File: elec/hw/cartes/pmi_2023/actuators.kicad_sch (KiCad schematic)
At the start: 39 parts, among them J1 con_servo, J2 con_servo, J3 con_servo, J4 con_servo, U17 SN74LVC2T45DCU, U21 SN74LVC2T45DCU, U23 PCA9685PW

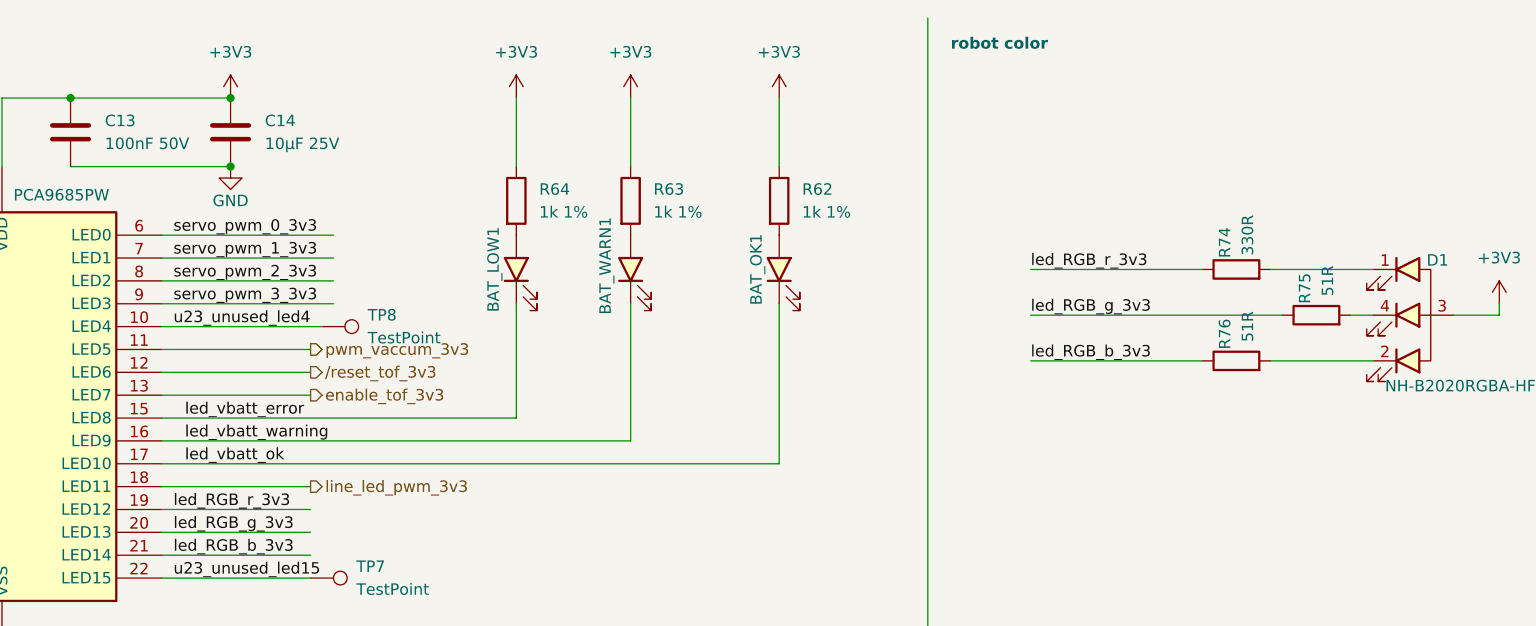
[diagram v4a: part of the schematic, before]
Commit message: bom updated and component selection optimized to decrease bom cost
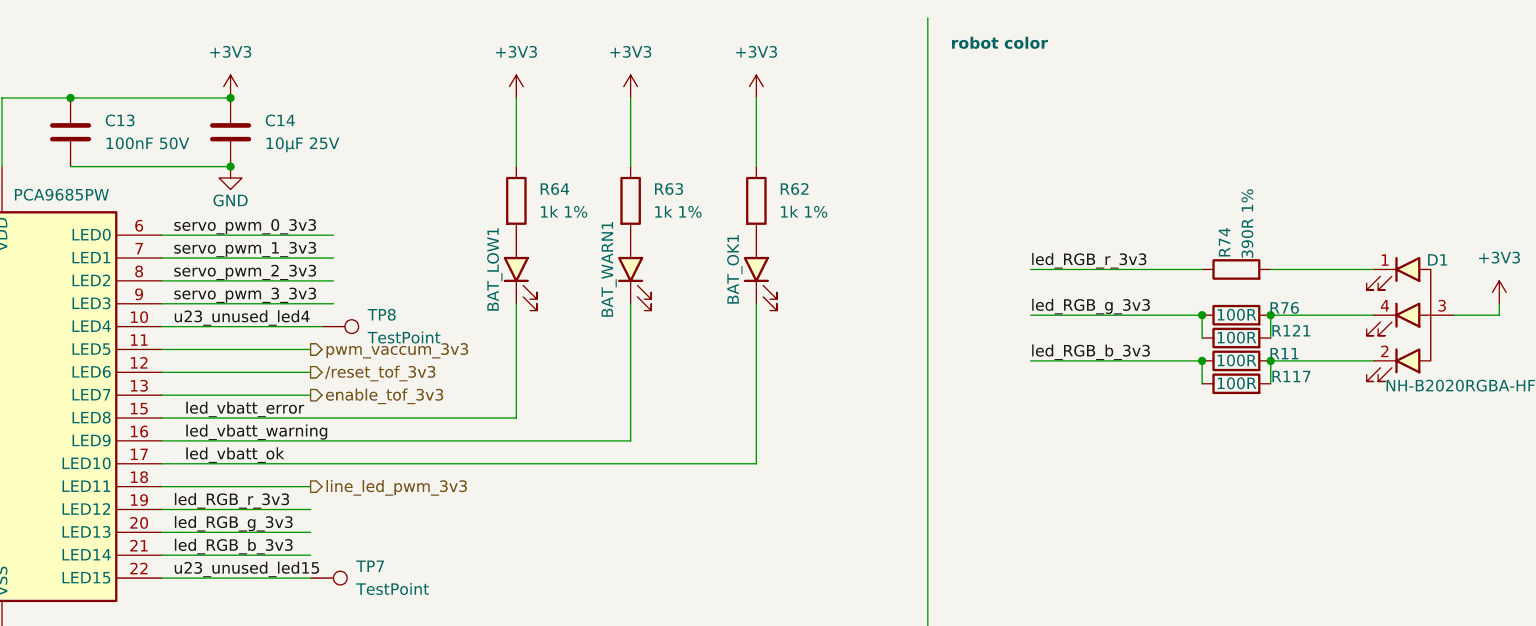
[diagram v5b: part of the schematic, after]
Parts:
- removed R75, R76: 51R, cocotter_resistor:r0603_reflow, symbol cocotter_resistors:R_51R_0603_1%
- added R11, R117, R121, R76: 100R, cocotter_resistor:r0603_reflow, symbol cocotter_resistors:R_100R_0603_1%
- BAT_OK1: value white, 0603 -> green, 0603; symbol cocotter_diodes:white_led_0603 -> cocotter_diodes:green_led_0603; DIGIKEY_REF (none) -> 3147-B19Y1UYG-20C000313U1930CT-ND; JLCPCB Part # C2290 -> C22371299; MOUSER_REF (none) -> 710-150060VS55040
- BAT_WARN1: value yellow, 0805 -> yellow, 0603; footprint cocotter_diodes:LED_0805_2012Metric -> cocotter_diodes:LED_0603_1608Metric; symbol cocotter_diodes:yellow_led_0805 -> cocotter_diodes:yellow_led_0603; JLCPCB Part # (none) -> C965802
- R74: value 330R -> 390R 1%; symbol cocotter_resistors:R_330R_0603_1% -> cocotter_resistors:R_390R_0603_1%; JLCPCB Part # C23138 -> C23151; Specification 330R 0603 1% 100mW -> 390R 0603 1% 100mW
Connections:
- net led_RGB_b_3v3: now also R11.1, R117.1
- net led_RGB_g_3v3: now also R121.1, R76.1
- net at D1.4 (C_GREEN): now also R121.2, R76.2
- net at D1.2 (C_BLUE): now also R11.2, R117.2
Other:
- moved on the sheet: BAT_OK1, R62

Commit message: first pass review corrections
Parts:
- removed BAT_LOW1: red, 0603, cocotter_diodes:LED_0603_1608Metric, symbol cocotter_diodes:red_led_0603
- removed BAT_OK1: green, 0603, cocotter_diodes:LED_0603_1608Metric, symbol cocotter_diodes:green_led_0603
- removed BAT_WARN1: yellow, 0603, cocotter_diodes:LED_0603_1608Metric, symbol cocotter_diodes:yellow_led_0603
- added BAT2: NH-B2020RGBA-HF, cocotter_diodes:NH-B2020RGBA-HF, symbol cocotter_diodes:NH-B2020RGBA-HF
- R62, R63: value 1k 1% -> 100R; symbol cocotter_resistors:R_1k_0603_1% -> cocotter_resistors:R_100R_0603_1%; JLCPCB Part # C2991540 -> C22775; Specification 10k 0603 1% 100mW -> 100R 0603 1% 100mW
- R64: value 1k 1% -> 390R 1%; symbol cocotter_resistors:R_1k_0603_1% -> cocotter_resistors:R_390R_0603_1%; JLCPCB Part # C2991540 -> C23151; Specification 10k 0603 1% 100mW -> 390R 0603 1% 100mW
- R74: value 390R 1% -> 100R; symbol cocotter_resistors:R_390R_0603_1% -> cocotter_resistors:R_100R_0603_1%; JLCPCB Part # C23151 -> C22775; Specification 390R 0603 1% 100mW -> 100R 0603 1% 100mW
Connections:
- net led_vbatt_error is gone; now on net led_vbatt_G: U23.15 (LED8)
- net led_vbatt_ok is gone; now on net led_vbatt_R: U23.17 (LED10)
- net led_vbatt_warning is gone; now on net led_vbatt_B: U23.16 (LED9)
- net +3V3: now also BAT2.3 (COM); no longer R62.1, R63.1, R64.1
- net led_vbatt_B: now reaches R62.2
- net led_vbatt_R: now reaches R64.2
- net led_vbatt_G: now reaches R63.2
- new net: BAT2.2 (C_BLUE), R62.1
- new net: BAT2.1 (C_RED), R64.1
- new net: BAT2.4 (C_GREEN), R63.1
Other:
- note added: "If is between 10 and 13mA, let it shine !!!"
- moved on the sheet: R62, R63, R64
